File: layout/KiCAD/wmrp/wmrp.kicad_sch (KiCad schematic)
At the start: 2 parts, among them U1 AD8552

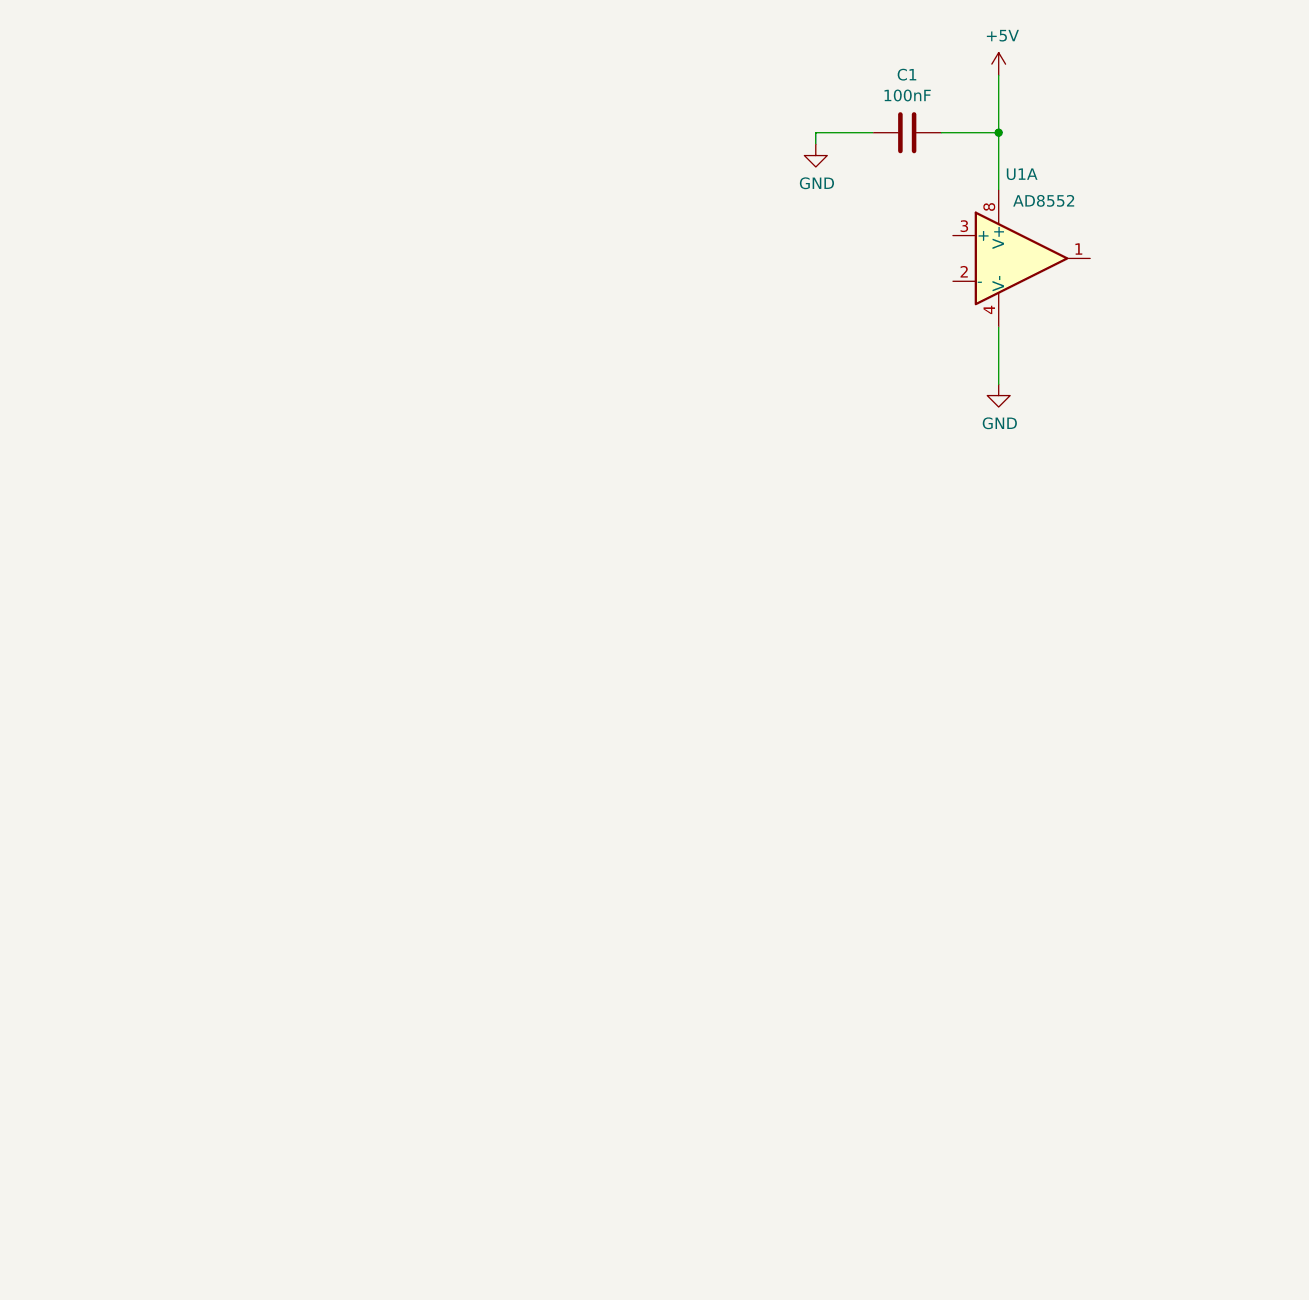
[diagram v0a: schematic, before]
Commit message: First try to use instrumentation amplifier for thermocouple reading
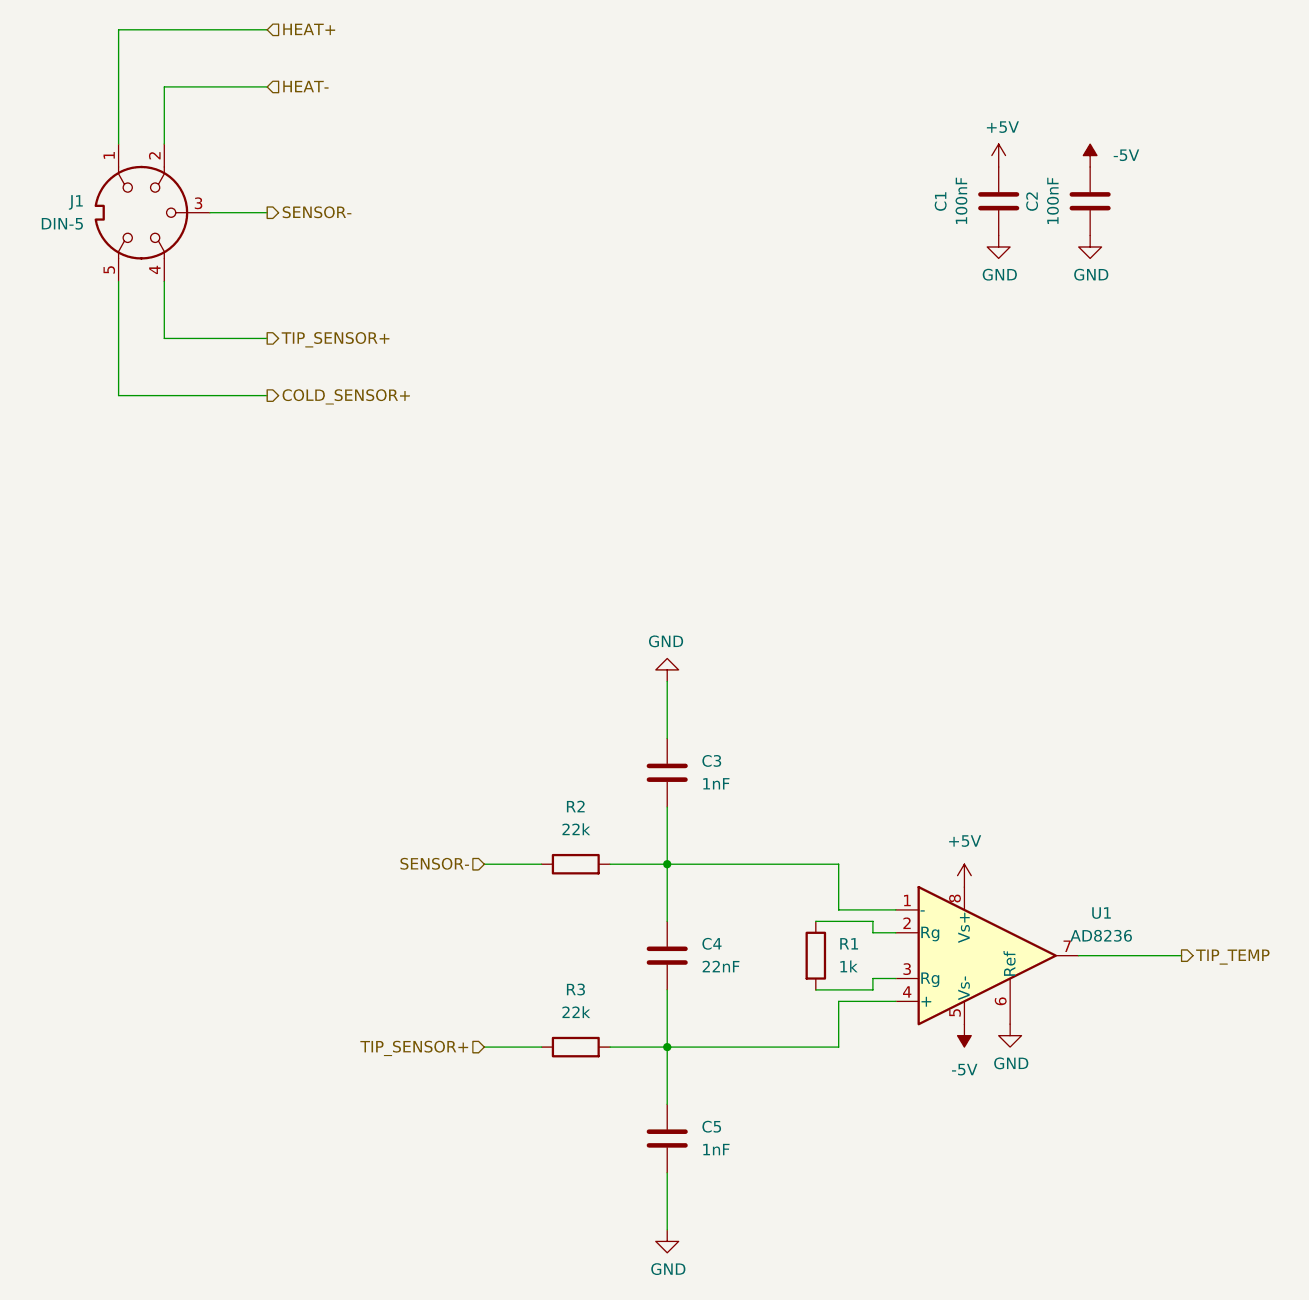
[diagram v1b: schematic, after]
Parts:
- removed U1: AD8552, Package_SO:SOIC-8_3.9x4.9mm_P1.27mm, symbol lm2904:AD8552
- added C2: 100nF, Capacitor_SMD:C_0805_2012Metric, symbol Device:C
- added C3, C5: 1nF, Capacitor_SMD:C_0603_1608Metric, symbol Device:C
- added C4: 22nF, Capacitor_SMD:C_0603_1608Metric, symbol Device:C
- added J1: DIN-5, Connector_PinHeader_2.54mm:PinHeader_1x05_P2.54mm_Vertical, symbol Connector:DIN-5
- added R1: 1k, Resistor_SMD:R_0603_1608Metric, symbol Device:R
- added R2, R3: 22k, Resistor_SMD:R_0603_1608Metric, symbol Device:R
- added U1: AD8236, Package_SO:MSOP-8_3x3mm_P0.65mm, symbol Amplifier_Instrumentation:AD8236
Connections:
- net +5V: now also U1.8 (Vs+)
- net GND: now also C2.2, C3.1, C5.2, U1.6 (Ref)
- new net: C3.2, C4.1, R2.2, U1.1 (-)
- new net: R1.1, U1.2 (Rg)
- new net: R1.2, U1.3 (Rg)
- new net: C4.2, C5.1, R3.2, U1.4 (+)
- new net -5V: C2.1, U1.5 (Vs-)
- new net COLD_SENSOR+: J1.5
- new net HEAT+: J1.1
- new net HEAT-: J1.2
- new net SENSOR-: J1.3, R2.1
- new net TIP_SENSOR+: J1.4, R3.1
- new net TIP_TEMP: U1.7
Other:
- moved on the sheet: C1
